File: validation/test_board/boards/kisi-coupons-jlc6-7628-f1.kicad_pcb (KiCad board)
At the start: 6 copper layers, 50 x 48 mm, 8 parts, among them J1 292-J-P-EP-ST-EL-01, J2 292-J-P-EP-ST-EL-01, J3 292-J-P-EP-ST-EL-01, J4 292-J-P-EP-ST-EL-01, J5 292-J-P-EP-ST-EL-01, J6 292-J-P-EP-ST-EL-01, J7 292-J-P-EP-ST-EL-01, J8 292-J-P-EP-ST-EL-01

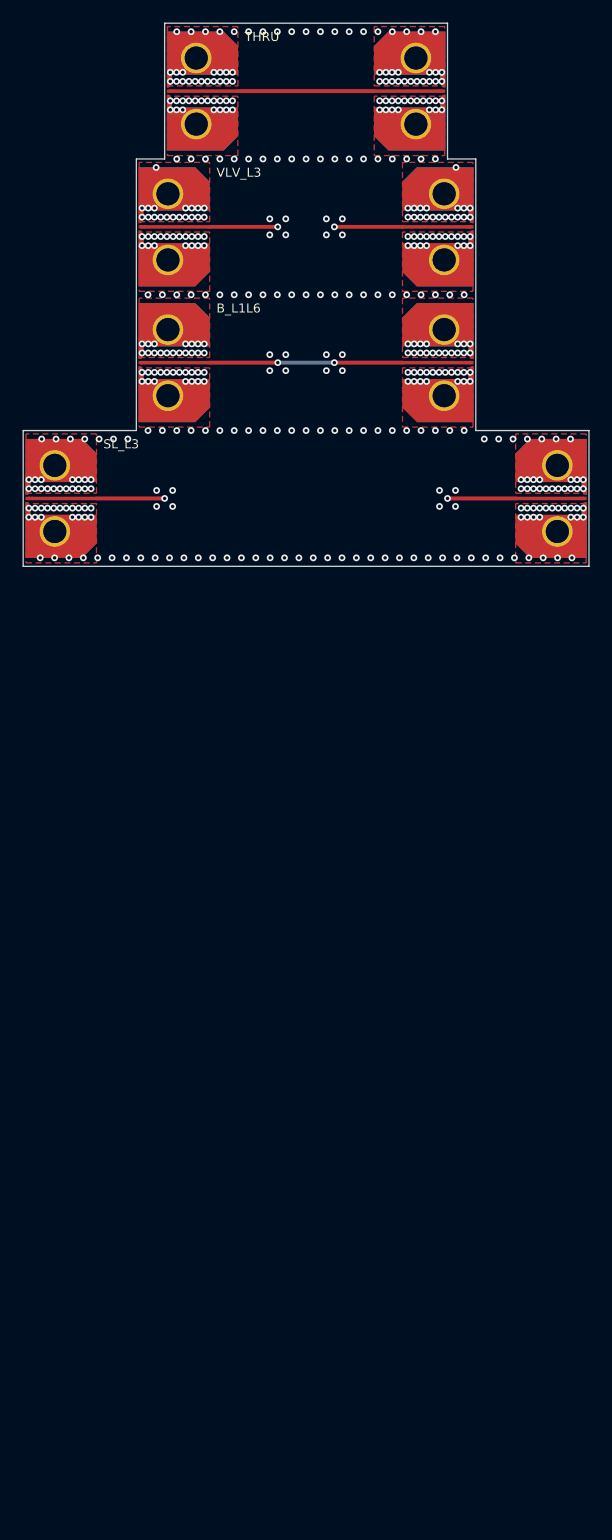
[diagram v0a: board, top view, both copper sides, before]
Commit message: First order: two 4-layer boards and one 6-layer board
- Maintainer's layout (2026-10-31): jlc4-7628-f1 100 x 96 mm (THRU,
  CPWG L / 2L, XT_MS, G_CAV), jlc4-7628-f2 35 x 156 mm (THRU, A x 3,
  D 0.7 / 2 mm / none, PAIR, E with 2 and 0 GND vias), jlc6-7628-f1
  50 x 132 mm (THRU, SL_L3 / VLV_L3, B_L1L6, PAIR, E_R_G2, D x 3). One
  2x-thru per board. An edge launch needs 12 mm of edge per connector
  and side, so the 4-layer set cannot share one 100 x 100 mm board; the
  two boards above their price bracket get their own size limits.
- DRC (KiCad 7, converted copies): no errors; kisi check rerun; the
  first-order table in test_board.md and README lists the exact sizes.

Co-Authored-By: Claude Opus 5.5 <noreply@anthropic.com>
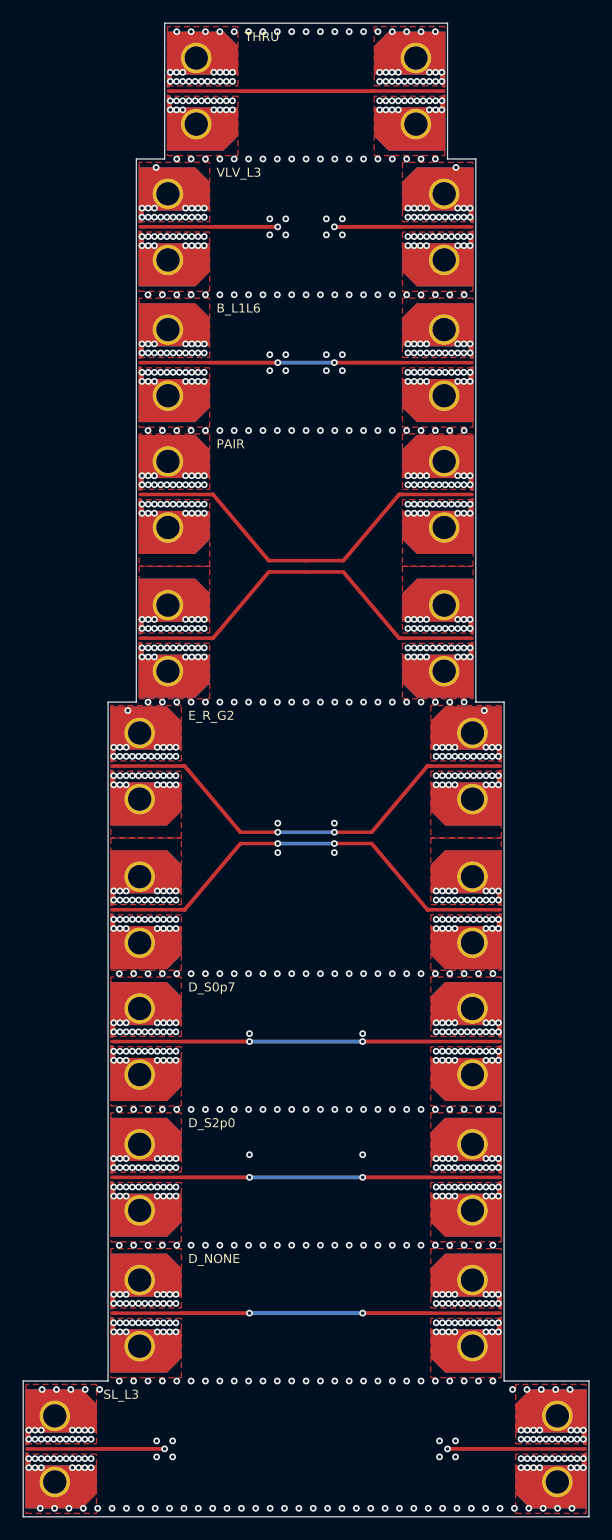
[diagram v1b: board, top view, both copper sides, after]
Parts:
- added J10: 292-J-P-EP-ST-EL-01, kisi_coupons:Samtec_292-J-P-EP-ST-EL-01_EdgeLaunch, F.Cu at (70.0, 84.3)
- added J11: 292-J-P-EP-ST-EL-01, kisi_coupons:Samtec_292-J-P-EP-ST-EL-01_EdgeLaunch, F.Cu at (37.5, 95.7)
- added J12: 292-J-P-EP-ST-EL-01, kisi_coupons:Samtec_292-J-P-EP-ST-EL-01_EdgeLaunch, F.Cu at (37.5, 108.3)
- added J13: 292-J-P-EP-ST-EL-01, kisi_coupons:Samtec_292-J-P-EP-ST-EL-01_EdgeLaunch, F.Cu at (72.5, 95.7)
- added J14: 292-J-P-EP-ST-EL-01, kisi_coupons:Samtec_292-J-P-EP-ST-EL-01_EdgeLaunch, F.Cu at (72.5, 108.3)
- added J15: 292-J-P-EP-ST-EL-01, kisi_coupons:Samtec_292-J-P-EP-ST-EL-01_EdgeLaunch, F.Cu at (37.5, 120.0)
- added J16: 292-J-P-EP-ST-EL-01, kisi_coupons:Samtec_292-J-P-EP-ST-EL-01_EdgeLaunch, F.Cu at (72.5, 120.0)
- added J17: 292-J-P-EP-ST-EL-01, kisi_coupons:Samtec_292-J-P-EP-ST-EL-01_EdgeLaunch, F.Cu at (37.5, 132.0)
- added J18: 292-J-P-EP-ST-EL-01, kisi_coupons:Samtec_292-J-P-EP-ST-EL-01_EdgeLaunch, F.Cu at (72.5, 132.0)
- added J19: 292-J-P-EP-ST-EL-01, kisi_coupons:Samtec_292-J-P-EP-ST-EL-01_EdgeLaunch, F.Cu at (37.5, 144.0)
- added J20: 292-J-P-EP-ST-EL-01, kisi_coupons:Samtec_292-J-P-EP-ST-EL-01_EdgeLaunch, F.Cu at (72.5, 144.0)
- added J21: 292-J-P-EP-ST-EL-01, kisi_coupons:Samtec_292-J-P-EP-ST-EL-01_EdgeLaunch, F.Cu at (30.0, 156.0)
- added J22: 292-J-P-EP-ST-EL-01, kisi_coupons:Samtec_292-J-P-EP-ST-EL-01_EdgeLaunch, F.Cu at (80.0, 156.0)
- added J9: 292-J-P-EP-ST-EL-01, kisi_coupons:Samtec_292-J-P-EP-ST-EL-01_EdgeLaunch, F.Cu at (70.0, 71.7)
- moved J8 41.9 mm to (40.0, 84.3), turned to 0 degrees
- moved J7 10.0 mm to (40.0, 71.7)
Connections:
- J7 pad 1: SE_SL_L3 -> DP_PAIR_P
- J8 pad 1: SE_SL_L3 -> DP_PAIR_N
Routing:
- net DP_E_R_G2_P: track 0.00 -> 38.8 mm, vias 0 -> 2
- net DP_E_R_G2_N: track 0.00 -> 38.8 mm, vias 0 -> 2
- net DP_PAIR_P: track 0.00 -> 33.8 mm
- net DP_PAIR_N: track 0.00 -> 33.8 mm
- net SE_D_S2p0: track 0.00 -> 33.4 mm, vias 0 -> 2
- net SE_D_S0p7: track 0.00 -> 33.4 mm, vias 0 -> 2
- net SE_D_NONE: track 0.00 -> 33.4 mm, vias 0 -> 2
- net GND: vias 450 -> 1091
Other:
- board size 50 x 48 mm -> 50 x 132 mm
- board text added: "2026-10-31"
- board text added: "D_NONE"
- board text added: "D_S0p7"
- board text added: "D_S2p0"
- board text added: "E_R_G2"
- board text added: "PAIR"
- board text added: "kisi-coupons-jlc6-7628-f1: kisi measurement coupons v3 (2026-10-31)"
- board text removed: "2026-10-30"
- board text removed: "kisi-coupons-jlc6-7628-f1: kisi measurement coupons v3 (2026-10-30)"

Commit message: Coupon boards: own zone priorities, project-local footprint library
- KiCad 8/9 DRC reported overlapping zones of equal priority (the GND
  pour rectangles on L1 meet at 4-port launch pairs and along the CPWG
  coupons: 78 pairs on 26 boards). Every zone now has its own priority
  (planes 0, pours 1, 2, ..., islands and patches above); an outline
  check finds no equal-priority overlap left.
- The footprints the boards use are written as a project-local library
  (boards/kisi_coupons.pretty + fp-lib-table with ${KIPRJMOD}): the
  Samtec launch per launch width, the capacitor land patterns, the IC
  pin fields; per-instance Port/Status fields dropped, so board and
  library match. DRC (KiCad 7 on converted copies, with the library):
  no library warnings, no errors; the first-order boards are clean.
- Boards regenerated, kisi check unchanged.

Co-Authored-By: Claude Opus 5.5 <noreply@anthropic.com>
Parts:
- removed the J17 at (37.5, 132.0)
- removed the J9 at (70.0, 71.7)
- added J15: 292-J-P-EP-ST-EL-01, kisi_coupons:Samtec_292-J-P-EP-ST-EL-01_EdgeLaunch_W0.315, F.Cu at (37.5, 120.0)
- added J8: 292-J-P-EP-ST-EL-01, kisi_coupons:Samtec_292-J-P-EP-ST-EL-01_EdgeLaunch_W0.315, F.Cu at (40.0, 84.3)
- J1, J10, J11, J12, J13, J14, J16, J18, J19, J2, J20, J21, J22, J3, J4, J5, J6, J7: footprint kisi_coupons:Samtec_292-J-P-EP-ST-EL-01_EdgeLaunch -> kisi_coupons:Samtec_292-J-P-EP-ST-EL-01_EdgeLaunch_W0.315
- J17: renamed from J15; footprint kisi_coupons:Samtec_292-J-P-EP-ST-EL-01_EdgeLaunch -> kisi_coupons:Samtec_292-J-P-EP-ST-EL-01_EdgeLaunch_W0.315
- J9: renamed from J8; footprint kisi_coupons:Samtec_292-J-P-EP-ST-EL-01_EdgeLaunch -> kisi_coupons:Samtec_292-J-P-EP-ST-EL-01_EdgeLaunch_W0.315
- moved J9 32.6 mm to (70.0, 71.7), turned to 180 degrees
- moved J17 12.0 mm to (37.5, 132.0)
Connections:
- J17 pad 1: SE_D_S0p7 -> SE_D_S2p0
- J9 pad 1: DP_PAIR_N -> DP_PAIR_P
